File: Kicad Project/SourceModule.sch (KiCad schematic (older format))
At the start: 33 parts, among them J1 Conn_01x02, J2 Conn_01x02, J3 Conn_01x02, J4 Conn_01x02, J5 Conn_01x02, J7 Conn_01x02, U5 AP1117-50, U6 GALI-2+, U7 RMK-3-93+, U8 GALI-2+

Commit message: PCB Edits post PDR
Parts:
- added C22: 1uF, Capacitors_SMD:C_0805, symbol C
- added C23: 470pF, Capacitors_SMD:C_0805, symbol C
- added C24: 10uF, Capacitors_SMD:C_0805, symbol C
- added R22, R23: 2K, Resistors_SMD:R_0603, symbol R
- added U16: TC1185, RadarComponents:SOT23-5, symbol TC1185
- C18, C20, C21: value C -> 10nF
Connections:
- net +3V3: now also C22.1, U16.5 (VOUT)
- net +5V: now also C24.1, U16.1 (Vin), U16.3 (~SHDN)
- net GND: now also J4.2 (Pin_2), C22.2, C23.2, C24.2, R23.2, U16.2 (GND); no longer J4.1 (Pin_1)
- net at VCO1.2 (TUNE): now also R22.1, R23.1; no longer J1.2 (Pin_2)
- net at R10.2, R11.1: now also J4.1 (Pin_1); no longer J4.2 (Pin_2)
- new net: J1.2 (Pin_2), R22.2
- new net: C23.1, U16.4 (Bypass)
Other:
- note removed: "3.3V from Teensy"

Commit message: Rev 1!
Gerbers Generated
Sent to Smart
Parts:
- removed C24: 10uF, Capacitors_SMD:C_0805, symbol C
- removed R15, R20: R, Resistors_SMD:R_0603, symbol R
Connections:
- net GND: now also U5.1 (GND)
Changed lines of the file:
@@
 $EndComp
 $Comp
-L +3.3V #PWR36
+L +3.3V #PWR020
 U 1 1 59F4A689
 P 3400 2550
-F 0 "#PWR36" H 3400 2400 50  0001 C CNN
+F 0 "#PWR020" H 3400 2400 50  0001 C CNN
 F 1 "+3.3V" H 3400 2690 50  0000 C CNN
 F 2 "" H 3400 2550 50  0001 C CNN
@@
 $EndComp
 $Comp
-L GND #PWR22
+L GND #PWR021
 U 1 1 59F4A990
 P 1050 1800
-F 0 "#PWR22" H 1050 1550 50  0001 C CNN
+F 0 "#PWR021" H 1050 1550 50  0001 C CNN
 F 1 "GND" H 1050 1650 50  0000 C CNN
 F 2 "" H 1050 1800 50  0001 C CNN
@@
 $EndComp
 $Comp
-L GND #PWR35
+L GND #PWR022
 U 1 1 59F4AA4C
 P 3200 3250
-F 0 "#PWR35" H 3200 3000 50  0001 C CNN
+F 0 "#PWR022" H 3200 3000 50  0001 C CNN
 F 1 "GND" H 3200 3100 50  0000 C CNN
 F 2 "" H 3200 3250 50  0001 C CNN
@@
 $EndComp
 $Comp
-L GND #PWR38
+L GND #PWR023
 U 1 1 59F4AA6C
 P 3600 3250
-F 0 "#PWR38" H 3600 3000 50  0001 C CNN
+F 0 "#PWR023" H 3600 3000 50  0001 C CNN
 F 1 "GND" H 3600 3100 50  0000 C CNN
 F 2 "" H 3600 3250 50  0001 C CNN
@@
 	3600 2600 3600 2950
 $Comp
-L GND #PWR34
+L GND #PWR024
 U 1 1 59F4AB52
 P 3150 1700
-F 0 "#PWR34" H 3150 1450 50  0001 C CNN
+F 0 "#PWR024" H 3150 1450 50  0001 C CNN
 F 1 "GND" H 3150 1550 50  0000 C CNN
 F 2 "" H 3150 1700 50  0001 C CNN
@@
 $EndComp
 $Comp
-L GND #PWR20
+L GND #PWR025
 U 1 1 59F4AE46
 P 850 2650
-F 0 "#PWR20" H 850 2400 50  0001 C CNN
+F 0 "#PWR025" H 850 2400 50  0001 C CNN
 F 1 "GND" H 850 2500 50  0000 C CNN
 F 2 "" H 850 2650 50  0001 C CNN
@@
 Frequency Feedback
 $Comp
-L GND #PWR50
+L GND #PWR026
 U 1 1 59F4B365
 P 7300 2900
-F 0 "#PWR50" H 7300 2650 50  0001 C CNN
+F 0 "#PWR026" H 7300 2650 50  0001 C CNN
 F 1 "GND" H 7300 2750 50  0000 C CNN
 F 2 "" H 7300 2900 50  0001 C CNN
@@
 Connection ~ 6000 2800
 $Comp
-L GND #PWR49
+L GND #PWR027
 U 1 1 59F7A17E
 P 6000 3250
-F 0 "#PWR49" H 6000 3000 50  0001 C CNN
+F 0 "#PWR027" H 6000 3000 50  0001 C CNN
 F 1 "GND" H 6000 3100 50  0000 C CNN
 F 2 "" H 6000 3250 50  0001 C CNN
@@
 $EndComp
 $Comp
-L GND #PWR43
+L GND #PWR028
 U 1 1 59F9EB1B
 P 4400 2650
-F 0 "#PWR43" H 4400 2400 50  0001 C CNN
+F 0 "#PWR028" H 4400 2400 50  0001 C CNN
 F 1 "GND" H 4400 2500 50  0000 C CNN
 F 2 "" H 4400 2650 50  0001 C CNN
@@
 	5800 1300 5800 1150
 $Comp
-L +9V #PWR45
+L +9V #PWR029
 U 1 1 59F9EF36
 P 5800 1150
-F 0 "#PWR45" H 5800 1000 50  0001 C CNN
+F 0 "#PWR029" H 5800 1000 50  0001 C CNN
 F 1 "+9V" H 5800 1290 50  0000 C CNN
 F 2 "" H 5800 1150 50  0001 C CNN
@@
 $EndComp
 $Comp
-L GND #PWR44
+L GND #PWR030
 U 1 1 59F9EFD4
 P 5600 1750
-F 0 "#PWR44" H 5600 1500 50  0001 C CNN
+F 0 "#PWR030" H 5600 1500 50  0001 C CNN
 F 1 "GND" H 5600 1600 50  0000 C CNN
 F 2 "" H 5600 1750 50  0001 C CNN
@@
 	10700 1300 10700 1150
 $Comp
-L +9V #PWR54
+L +9V #PWR031
 U 1 1 59F9F432
 P 10700 1150
-F 0 "#PWR54" H 10700 1000 50  0001 C CNN
+F 0 "#PWR031" H 10700 1000 50  0001 C CNN
 F 1 "+9V" H 10700 1290 50  0000 C CNN
 F 2 "" H 10700 1150 50  0001 C CNN
@@
 $EndComp
 $Comp
-L GND #PWR53
+L GND #PWR032
 U 1 1 59F9F438
 P 10500 1750
-F 0 "#PWR53" H 10500 1500 50  0001 C CNN
+F 0 "#PWR032" H 10500 1500 50  0001 C CNN
 F 1 "GND" H 10500 1600 50  0000 C CNN
 F 2 "" H 10500 1750 50  0001 C CNN
@@
 $EndComp
 $Comp
-L GND #PWR52
+L GND #PWR033
 U 1 1 59F9F88B
 P 9350 2650
-F 0 "#PWR52" H 9350 2400 50  0001 C CNN
+F 0 "#PWR033" H 9350 2400 50  0001 C CNN
 F 1 "GND" H 9350 2500 50  0000 C CNN
 F 2 "" H 9350 2650 50  0001 C CNN
@@
 	8000 2200 8350 2200
 $Comp
-L GND #PWR51
+L GND #PWR034
 U 1 1 5A020DEA
 P 8200 2200
-F 0 "#PWR51" H 8200 1950 50  0001 C CNN
+F 0 "#PWR034" H 8200 1950 50  0001 C CNN
 F 1 "GND" H 8200 2050 50  0000 C CNN
 F 2 "" H 8200 2200 50  0001 C CNN
@@
 $EndComp
 $Comp
-L GND #PWR21
+L GND #PWR035
 U 1 1 5A026C05
 P 900 2300
-F 0 "#PWR21" H 900 2050 50  0001 C CNN
+F 0 "#PWR035" H 900 2050 50  0001 C CNN
 F 1 "GND" H 900 2150 50  0000 C CNN
 F 2 "" H 900 2300 50  0001 C CNN
@@
 $EndComp
 $Comp
-L GND #PWR26
+L GND #PWR036
 U 1 1 5A0270B6
 P 2050 4400
-F 0 "#PWR26" H 2050 4150 50  0001 C CNN
+F 0 "#PWR036" H 2050 4150 50  0001 C CNN
 F 1 "GND" H 2050 4250 50  0000 C CNN
 F 2 "" H 2050 4400 50  0001 C CNN
@@
 $EndComp
 $Comp
-L GND #PWR27
+L GND #PWR037
 U 1 1 5A02710F
 P 2050 4850
-F 0 "#PWR27" H 2050 4600 50  0001 C CNN
+F 0 "#PWR037" H 2050 4600 50  0001 C CNN
 F 1 "GND" H 2050 4700 50  0000 C CNN
 F 2 "" H 2050 4850 50  0001 C CNN
@@
 $EndComp
 $Comp
-L +3.3V #PWR30
+L +3.3V #PWR038
 U 1 1 5A027182
 P 2400 4750
-F 0 "#PWR30" H 2400 4600 50  0001 C CNN
+F 0 "#PWR038" H 2400 4600 50  0001 C CNN
 F 1 "+3.3V" H 2400 4890 50  0000 C CNN
 F 2 "" H 2400 4750 50  0001 C CNN
@@
 $EndComp
 $Comp
-L +9V #PWR29
+L +9V #PWR039
 U 1 1 5A027267
 P 2350 4300
-F 0 "#PWR29" H 2350 4150 50  0001 C CNN
+F 0 "#PWR039" H 2350 4150 50  0001 C CNN
 F 1 "+9V" H 2350 4440 50  0000 C CNN
 F 2 "" H 2350 4300 50  0001 C CNN
@@
 $EndComp
 $Comp
-L R R15
-U 1 1 5A04CBED
-P 2650 6500
-F 0 "R15" V 2730 6500 50  0000 C CNN
-F 1 "R" V 2650 6500 50  0000 C CNN
-F 2 "Resistors_SMD:R_0603" V 2580 6500 50  0001 C CNN
-F 3 "" H 2650 6500 50  0001 C CNN
-	1    2650 6500
-	1    0    0    -1
-$EndComp
-$Comp
-L R R20
-U 1 1 5A04CCA0
-P 3200 6100
-F 0 "R20" V 3280 6100 50  0000 C CNN
-F 1 "R" V 3200 6100 50  0000 C CNN
-F 2 "Resistors_SMD:R_0603" V 3130 6100 50  0001 C CNN
-F 3 "" H 3200 6100 50  0001 C CNN
-	1    3200 6100
-	1    0    0    -1
-$EndComp
-$Comp
 L C C19
 U 1 1 5A04CD36
@@
 $EndComp
 $Comp
-L +5V #PWR39
+L +5V #PWR040
 U 1 1 5A04CEA6
 P 3800 5900
-F 0 "#PWR39" H 3800 5750 50  0001 C CNN
+F 0 "#PWR040" H 3800 5750 50  0001 C CNN
 F 1 "+5V" H 3800 6040 50  0000 C CNN
 F 2 "" H 3800 5900 50  0001 C CNN
@@
 	3550 5950 3550 5900
 Connection ~ 3550 5900
-Wire Wire Line
-	3200 5950 3200 5900
 Connection ~ 3200 5900
 Wire Wire Line
 	2650 6200 2650 6350
-Wire Wire Line
-	2650 6300 3200 6300
-Wire Wire Line
-	3200 6300 3200 6250
-Connection ~ 2650 6300
 Wire Wire Line
 	1750 5900 2350 5900
@@
 Connection ~ 2000 5900
 $Comp
-L GND #PWR37
+L GND #PWR041
 U 1 1 5A04D587
 P 3550 6250
-F 0 "#PWR37" H 3550 6000 50  0001 C CNN
+F 0 "#PWR041" H 3550 6000 50  0001 C CNN
 F 1 "GND" H 3550 6100 50  0000 C CNN
 F 2 "" H 3550 6250 50  0001 C CNN
@@
 $EndComp
 $Comp
-L GND #PWR33
+L GND #PWR042
 U 1 1 5A04D65D
-P 2650 6650
-F 0 "#PWR33" H 2650 6400 50  0001 C CNN
-F 1 "GND" H 2650 6500 50  0000 C CNN
-F 2 "" H 2650 6650 50  0001 C CNN
-F 3 "" H 2650 6650 50  0001 C CNN
-	1    2650 6650
-	1    0    0    -1
-$EndComp
-$Comp
-L GND #PWR25
+P 2650 6350
+F 0 "#PWR042" H 2650 6100 50  0001 C CNN
+F 1 "GND" H 2650 6200 50  0000 C CNN
+F 2 "" H 2650 6350 50  0001 C CNN
+F 3 "" H 2650 6350 50  0001 C CNN
+	1    2650 6350
+	1    0    0    -1
+$EndComp
+$Comp
+L GND #PWR043
 U 1 1 5A04D6C5
 P 2000 6300
-F 0 "#PWR25" H 2000 6050 50  0001 C CNN
+F 0 "#PWR043" H 2000 6050 50  0001 C CNN
 F 1 "GND" H 2000 6150 50  0000 C CNN
 F 2 "" H 2000 6300 50  0001 C CNN
@@
 $EndComp
 $Comp
-L +9V #PWR24
+L +9V #PWR044
 U 1 1 5A04DB89
 P 1750 5900
-F 0 "#PWR24" H 1750 5750 50  0001 C CNN
+F 0 "#PWR044" H 1750 5750 50  0001 C CNN
 F 1 "+9V" H 1750 6040 50  0000 C CNN
 F 2 "" H 1750 5900 50  0001 C CNN
@@
 	2000 3750 2100 3750
 $Comp
-L GND #PWR28
+L GND #PWR045
 U 1 1 5A026C58
 P 2100 3750
-F 0 "#PWR28" H 2100 3500 50  0001 C CNN
+F 0 "#PWR045" H 2100 3500 50  0001 C CNN
 F 1 "GND" H 2100 3600 50  0000 C CNN
 F 2 "" H 2100 3750 50  0001 C CNN
@@
 $EndComp
 $Comp
-L +5V #PWR31
+L +5V #PWR046
 U 1 1 5A04E6CC
 P 2400 5250
-F 0 "#PWR31" H 2400 5100 50  0001 C CNN
+F 0 "#PWR046" H 2400 5100 50  0001 C CNN
 F 1 "+5V" H 2400 5390 50  0000 C CNN
 F 2 "" H 2400 5250 50  0001 C CNN
@@
 $EndComp
 $Comp
-L GND #PWR32
+L GND #PWR047
 U 1 1 5A04E737
 P 2400 5350
-F 0 "#PWR32" H 2400 5100 50  0001 C CNN
+F 0 "#PWR047" H 2400 5100 50  0001 C CNN
 F 1 "GND" H 2400 5200 50  0000 C CNN
 F 2 "" H 2400 5350 50  0001 C CNN
@@
 $EndComp
 $Comp
-L GND #PWR23
+L GND #PWR048
 U 1 1 5A051D90
 P 1500 2900
-F 0 "#PWR23" H 1500 2650 50  0001 C CNN
+F 0 "#PWR048" H 1500 2650 50  0001 C CNN
 F 1 "GND" H 1500 2750 50  0000 C CNN
 F 2 "" H 1500 2900 50  0001 C CNN
@@
 $EndComp
 $Comp
-L +5V #PWR42
+L +5V #PWR049
 U 1 1 5A05E9CE
 P 4200 6250
-F 0 "#PWR42" H 4200 6100 50  0001 C CNN
+F 0 "#PWR049" H 4200 6100 50  0001 C CNN
 F 1 "+5V" H 4200 6390 50  0000 C CNN
 F 2 "" H 4200 6250 50  0001 C CNN
@@
 $EndComp
 $Comp
-L GND #PWR40
+L GND #PWR050
 U 1 1 5A05F150
 P 4150 6750
-F 0 "#PWR40" H 4150 6500 50  0001 C CNN
+F 0 "#PWR050" H 4150 6500 50  0001 C CNN
 F 1 "GND" H 4150 6600 50  0000 C CNN
 F 2 "" H 4150 6750 50  0001 C CNN
@@
 $EndComp
 $Comp
-L +5V #PWR41
+L +5V #PWR051
 U 1 1 5A05FB12
 P 4150 7150
-F 0 "#PWR41" H 4150 7000 50  0001 C CNN
+F 0 "#PWR051" H 4150 7000 50  0001 C CNN
 F 1 "+5V" H 4150 7290 50  0000 C CNN
 F 2 "" H 4150 7150 50  0001 C CNN
@@
 	5800 6250 5950 6250
 $Comp
-L GND #PWR47
+L GND #PWR052
 U 1 1 5A0604B4
 P 5950 6550
-F 0 "#PWR47" H 5950 6300 50  0001 C CNN
+F 0 "#PWR052" H 5950 6300 50  0001 C CNN
 F 1 "GND" H 5950 6400 50  0000 C CNN
 F 2 "" H 5950 6550 50  0001 C CNN
@@
 $EndComp
 $Comp
-L GND #PWR48
+L GND #PWR053
 U 1 1 5A06054F
 P 5950 7450
-F 0 "#PWR48" H 5950 7200 50  0001 C CNN
+F 0 "#PWR053" H 5950 7200 50  0001 C CNN
 F 1 "GND" H 5950 7300 50  0000 C CNN
 F 2 "" H 5950 7450 50  0001 C CNN
@@
 $EndComp
 $Comp
-L +3.3V #PWR46
+L +3.3V #PWR054
 U 1 1 5A063648
 P 5950 6250
-F 0 "#PWR46" H 5950 6100 50  0001 C CNN
+F 0 "#PWR054" H 5950 6100 50  0001 C CNN
 F 1 "+3.3V" H 5950 6390 50  0000 C CNN
 F 2 "" H 5950 6250 50  0001 C CNN
@@
 Wire Wire Line
 	1000 2200 900  2200
-$Comp
-L C C24
-U 1 1 5A06094F
-P 4275 6400
-F 0 "C24" H 4300 6500 50  0000 L CNN
-F 1 "10uF" H 4300 6300 50  0000 L CNN
-F 2 "Capacitors_SMD:C_0805" H 4313 6250 50  0001 C CNN
-F 3 "" H 4275 6400 50  0001 C CNN
-	1    4275 6400
-	1    0    0    -1
-$EndComp
 Wire Wire Line
 	4200 6250 4400 6250
 Connection ~ 4275 6250
-Wire Wire Line
-	4275 6550 4275 6700
 Connection ~ 4275 6700
 Wire Wire Line

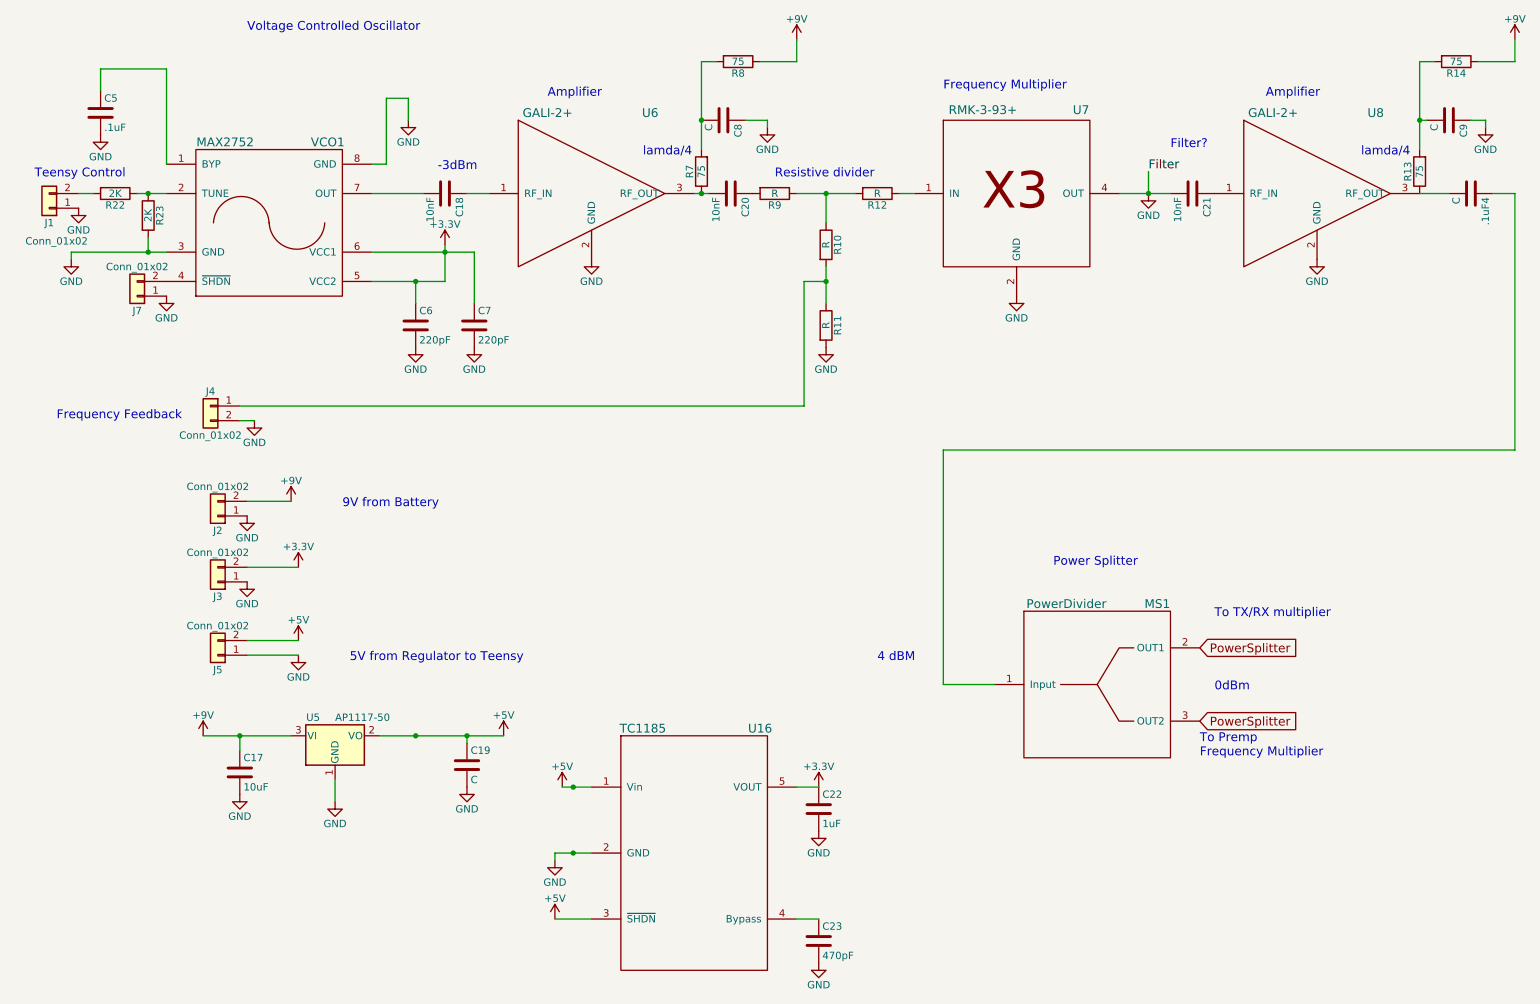
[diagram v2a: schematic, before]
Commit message: Rev 2 update 1
Changes for Rev2:
Mounting Holes (duh)
Right Headers
HeadphoneJack
Added tantulum Caps at Regulators
Added UFL conns
Removed Resistive Divider
&
General layout stuff
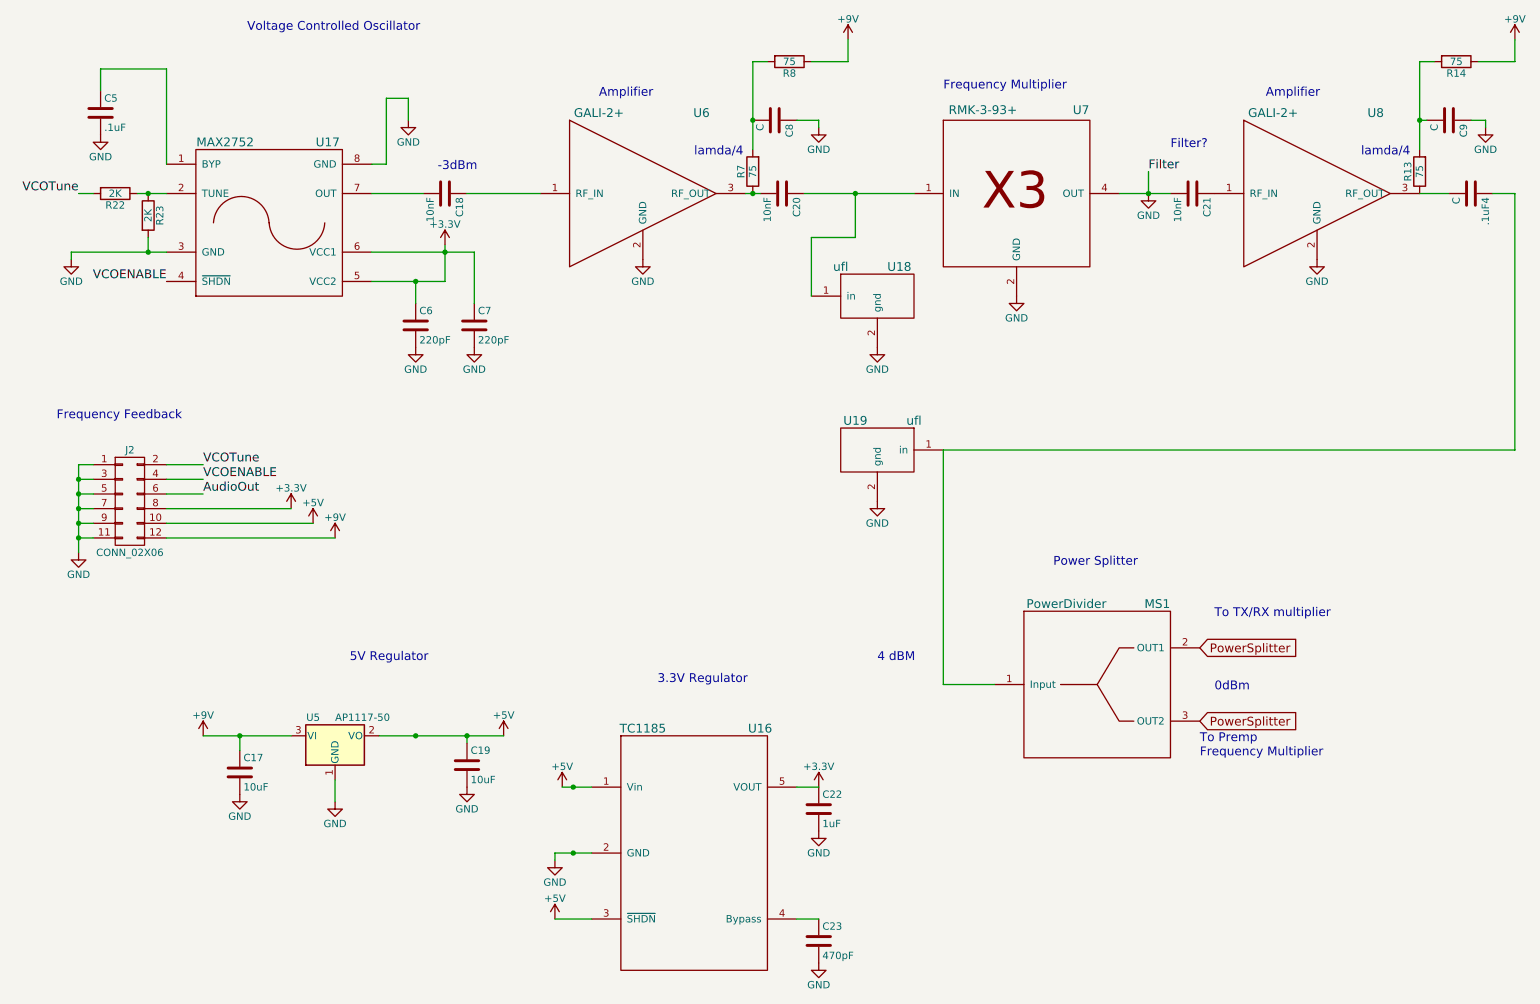
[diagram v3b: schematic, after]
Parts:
- removed J1, J2, J3, J5, J7: Conn_01x02, Pin_Headers:Pin_Header_Straight_1x02_Pitch1.27mm, symbol Conn_01x02
- removed J4: Conn_01x02, RadarComponents:UFL, symbol Conn_01x02
- removed R10, R11, R12, R9: R, RadarComponents:100PAD, symbol R
- added J2: CONN_02X06, Pin_Headers:Pin_Header_Straight_2x06_Pitch2.54mm, symbol CONN_02X06
- added U18, U19: ufl, RadarComponents:UFL, symbol ufl
- C19: value C -> 10uF; footprint Capacitors_SMD:C_0805 -> Capacitors_SMD:C_1210_HandSoldering
- C22: footprint Capacitors_SMD:C_0805 -> Capacitors_SMD:C_1210_HandSoldering
- renumbered VCO1 to U17
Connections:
- net +3V3: now also J2.8 (P8)
- net +5V: now also J2.10 (P10)
- net +9V: now also J2.12 (P12)
- net GND: now also J2.1 (P1), J2.11 (P11), J2.3 (P3), J2.5 (P5), J2.7 (P7), J2.9 (P9), U18.2 (gnd), U19.2 (gnd)
- net VCOENABLE: now reaches U17.4 (~SHDN)
- net VCOENABLE: now also J2.4 (P4)
- net at U7.1 (IN): now also C20.1, U18.1 (in)
- net at .1uF4.1, MS1.1 (Input): now also U19.1 (in)
- net VCOTune: now reaches R22.2
- net VCOTune: now also J2.2 (P2)
- new net AudioOut: J2.6 (P6)
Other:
- note added: "3.3V Regulator\n"
- note added: "5V Regulator\n"
- note removed: "5V from Regulator to Teensy"
- note removed: "9V from Battery\n"
- note removed: "Resistive divider"
- note removed: "Teensy Control"
- moved on the sheet: C20, C8, R7, R8, U6

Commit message: More Routing
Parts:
- U6: value GALI-2+ -> LEE-39+; symbol GALI-2+-RESCUE-Radar -> LEE-39+
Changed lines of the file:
@@
 -3dBm
 $Comp
-L GALI-2+-RESCUE-Radar U6
+L LEE-39+ U6
 U 1 1 59F9E96F
 P 4750 2200
 F 0 "U6" H 5150 2750 60  0000 C CNN
-F 1 "GALI-2+" H 4450 2750 60  0000 C CNN
+F 1 "LEE-39+" H 4450 2750 60  0000 C CNN
 F 2 "RadarComponents:Amplifier" H 4750 2200 60  0001 C CNN
 F 3 "" H 4750 2200 60  0001 C CNN
@@
 Text Label 1750 4150 0    60   ~ 0
 VCOENABLE
-Text Label 1750 4250 0    60   ~ 0
-AudioOut
 Wire Wire Line
 	6600 2200 5850 2200
@@
 Text Label 1500 2800 2    60   ~ 0
 VCOENABLE
+Text GLabel 1750 4250 2    60   Input ~ 0
+AudioOut
 $EndSCHEMATC
